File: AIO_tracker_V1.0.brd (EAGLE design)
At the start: 47 x 99.8 mm, 52 parts, among them J1 AVR_SPI_PRG_6PTH, Q1 MOSFET-PCHANNELSMD, U2 USD-SOCKETNEW

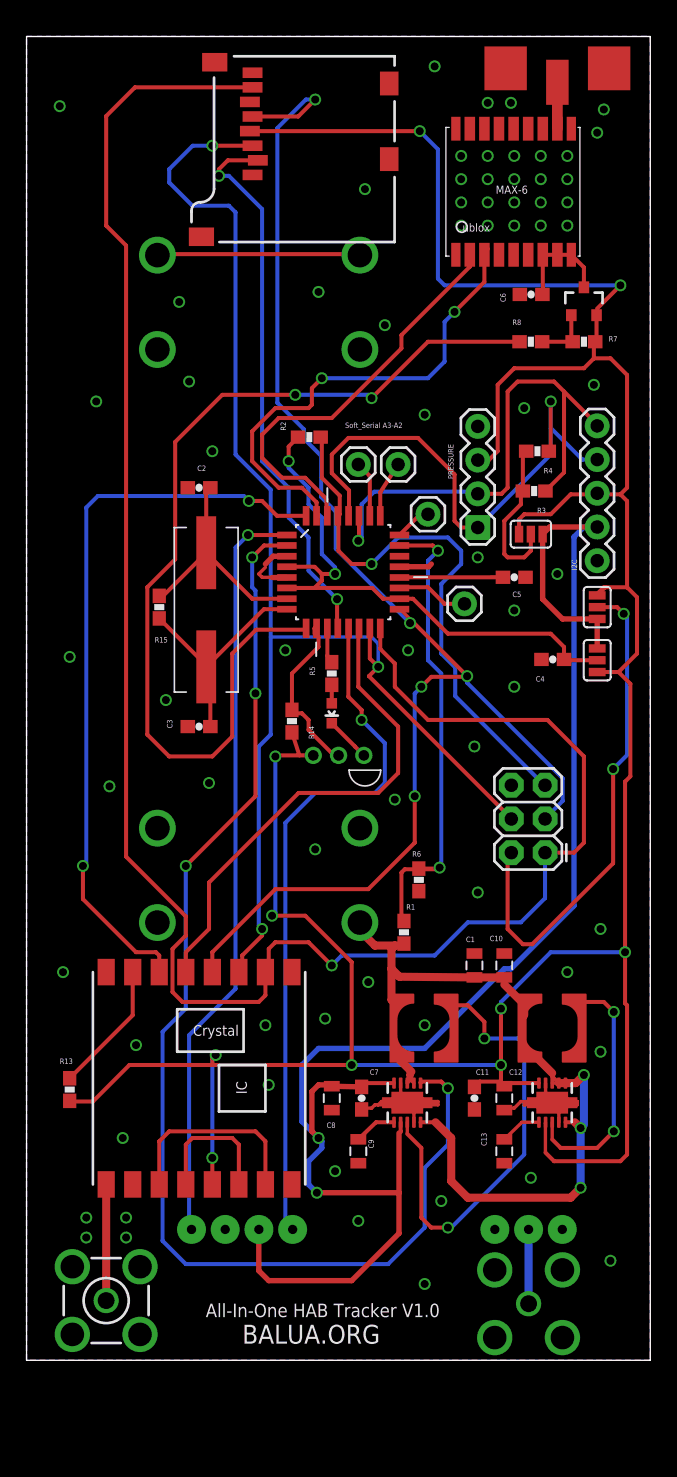
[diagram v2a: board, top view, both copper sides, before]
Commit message: Added extra power pins (5V, 3.3V and GND) and more
Added extra power pins (5V, 3.3V and GND)
Added I2C to Ublox
Placed smd jumpers in both I2C and RX/TX of Ublox for hardware selection
of communication mode.
Added pins for external RX/TX communication with arduino.
PCB layout updated
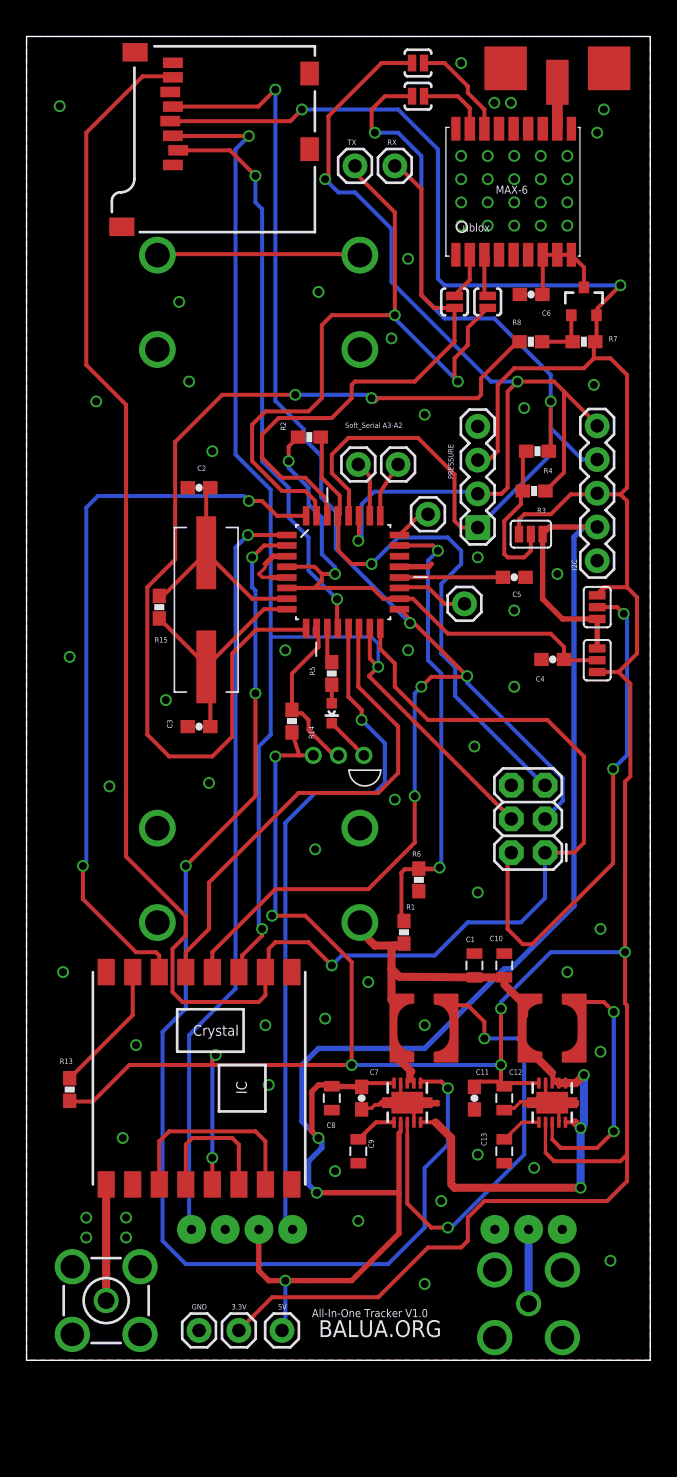
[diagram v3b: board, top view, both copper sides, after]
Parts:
- added 3.3V, 5V, GND, RX, TX: M01PTH, SparkFun-Connectors:1X01
- added SJ1, SJ3, SJ5, SJ6: SOLDERJUMPERNO, SparkFun-Passives:SJ_2S-NO
- moved U2 6.05 mm to (20.7, 80.3)
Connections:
- net D3 renamed SD_CS
- net D4 renamed TEMP
- new net N$11: SJ5.1, U$1.3_RXD1
- new net N$12: SJ6.1, U$1.2_TXD1
- new net N$15: SJ1.2, U$1.16_SDA2
- new net N$16: SJ3.2, U$1.17_SCL2
- net 3.3V: now also 3.3V.1
- net 5V: now also 5V.1
- net GND: now also GND.1
- net SCL: now also SJ3.1
- net SDA: now also SJ1.1
- net UBLOX_RXD: now also SJ5.2, TX.1; no longer U$1.3_RXD1
- net UBLOX_TXD: now also RX.1, SJ6.2; no longer U$1.2_TXD1
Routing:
- net 3.3V: track 250.9 -> 294.9 mm
- net SDA: track 40.5 -> 76.5 mm, vias 1 -> 3
- net SCL: track 43.6 -> 77.9 mm, vias 1 -> 2
- net UBLOX_RXD: track 36.7 -> 53.5 mm
- net UBLOX_TXD: track 31.6 -> 43.4 mm
- net N$15: track 0.00 -> 8.01 mm
- net N$16: track 0.00 -> 5.37 mm
- net MISO: track 150.2 -> 146.0 mm
- net N$11: track 0.00 -> 3.86 mm
- net 5V: track 123.3 -> 127.1 mm, vias 2 -> 3
- net N$12: track 0.00 -> 3.79 mm
- net SCK: track 108.0 -> 110.2 mm
- net MOSI: track 103.1 -> 101.1 mm
- net SD_CS: track 42.0 -> 43.3 mm
- net GPSEN: track 72.5 -> 73.5 mm
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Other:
- board text added: "All-In-One Tracker V1.0"
- board text removed: "All-In-One HAB Tracker V1.0"

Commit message: Updated library and erros
- Ava library updated
- SDN pin of the RFM22b connected to A6 instead of always HIGH
- Updated Sarantel Antenna Footprint
- A7 to external pin
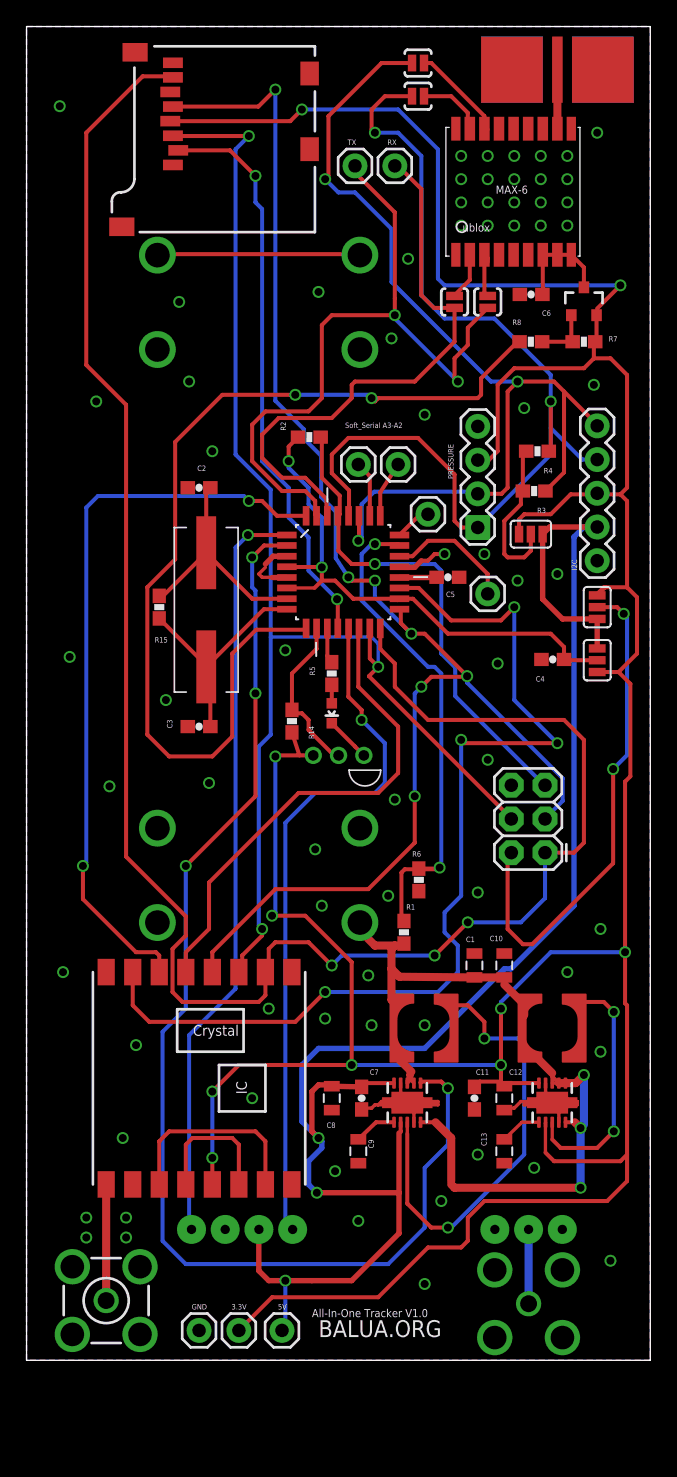
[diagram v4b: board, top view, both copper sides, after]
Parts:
- removed R13: 4.7k, SparkFun-Passives:0603-RES
- C2, C3: value 0.1uF -> 22pF
- R15: value 100k -> 1M
- U$2: value SARANTEL-SL1250 -> JDGA-REMQV-ANTENNA; device Ava:SARANTEL-SL1250 -> Ava:JDGA-RIGID_COMBO_PAD
- moved C5 5.00 mm to (30.8, 40.2)
- moved U$2 2.25 mm to (39.0, 78.5)
- moved JP7 1.90 mm to (33.8, 39.0)
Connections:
- removed net N$27: R13.2, U$7.15
- new net A7: JP7.1, U1.22
- net 3.3V: no longer R13.1
- net A6: now also U$7.15; no longer JP7.1
- net GND: now also U$2.P$2, U$2.P$4, U$2.P$5; no longer U$2.P$1
- net N$3: now also U$2.P$1; no longer U$2.P$2
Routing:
- net A6: track 5.44 -> 76.5 mm, vias 0 -> 4
- net 3.3V: track 294.9 -> 280.1 mm
- net N$27: track 9.97 -> 0.00 mm
- net A7: track 0.00 -> 9.67 mm
- net N$4: track 8.70 -> 2.80 mm
- net RESET: track 41.8 -> 37.1 mm
- net N$8: track 46.8 -> 42.7 mm
- net SCK: track 110.2 -> 112.4 mm, vias 5 -> 7
- net VBATTADC: track 36.4 -> 38.2 mm
- net GND: track 38.0 -> 39.4 mm, vias 72 -> 71
- net N$3: track 3.50 -> 4.45 mm
- net MISO: track 146.0 -> 146.7 mm, vias 1 -> 3
- net N$15: track 8.01 -> 7.43 mm
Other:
- board size 47 x 99.8 mm -> 47 x 100.5 mm

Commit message: Added NTX2 Support option
Added NTX2 Support option and finished routing
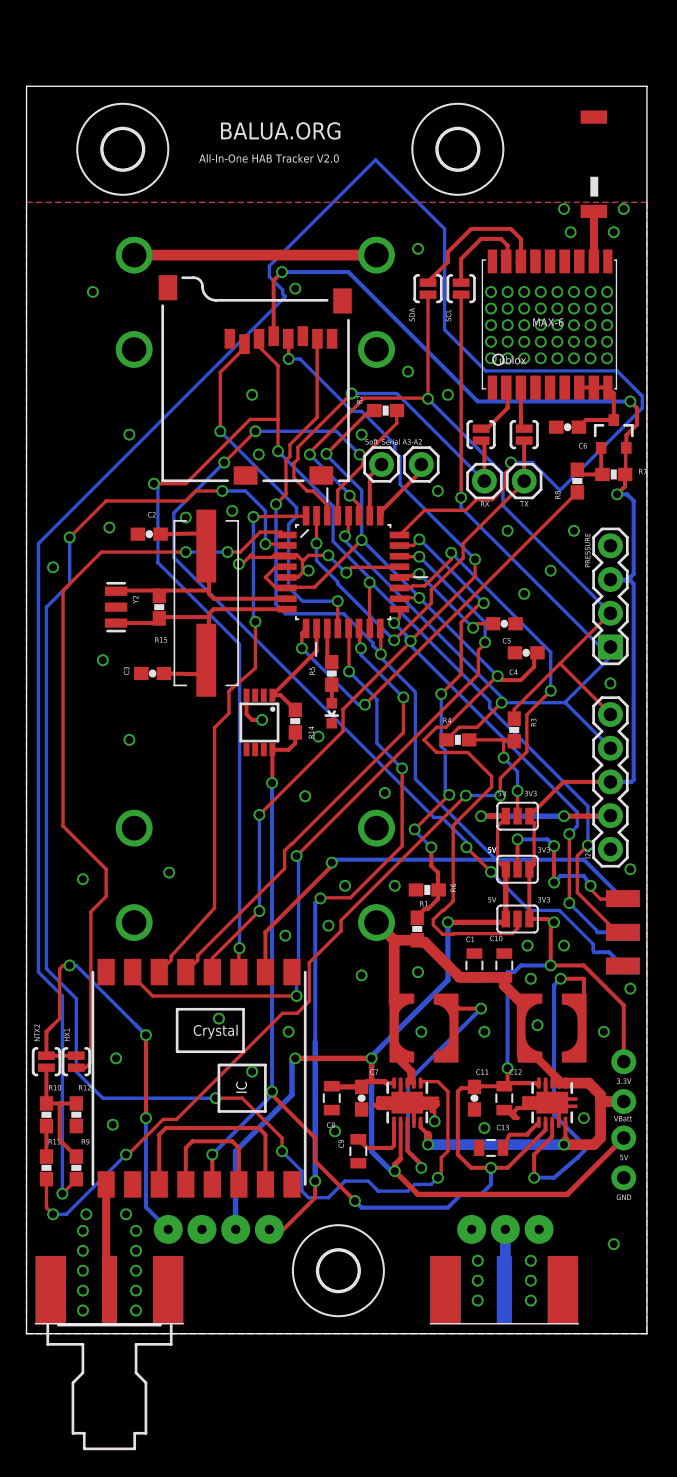
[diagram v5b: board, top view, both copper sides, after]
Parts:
- removed JP4, JP7: M01PTH, SparkFun-Connectors:1X01
- added R10, R11, R12, R9: 10k, SparkFun-Passives:0603-RES
- added SJ2, SJ4: SOLDERJUMPERNO, SparkFun-Passives:SJ_2S-NO
- added U$10, U$11: (no value), holes:3,0
- added VBATT: M01SMDNS, SparkFun-Connectors:1X01NS
- added X1: SMA-142-0701-881/886, con-coax:J502-ND-142-0701-881/886
- added Y2: 16MHz, SparkFun-FreqCtrl:RESONATOR-SMD
- 3.3V, 5V, GND: value M01PTH -> M01SMDNS; device SparkFun-Connectors:1X01 -> SparkFun-Connectors:1X01NS
- J1: value AVR_SPI_PRG_6PTH -> EDGE_ICSP; device SparkFun-Connectors:2X3 -> Ava:EDGE_MOUNTED_ICSP
- JP2, JP3: value JUMPER-3SMD -> (none)
- U$2: value JDGA-REMQV-ANTENNA -> JTI_ANTENNA-1575AT43A40; device Ava:JDGA-RIGID_COMBO_PAD -> Ava:JTI_ANTENNA-1575AT43A40
- U$5: value BUS-SMA -> (none); device Ava:BUS-SMA -> holes:3,0
- U$8: value BUS-SMA -> SMA-142-0701-881/886; device Ava:BUS-SMA -> con-coax:J502-ND-142-0701-881/886
- U$9: value DS1820TO92 -> DS1820; device Ava:DS1820 -> Ava:µSOP8
- moved U$5 87.2 mm to (31.5, 72.5), flipped to the top
- moved 3.3V 35.4 mm to (44.0, 3.75)
- moved GND 34.0 mm to (44.0, -5.00)
- moved U2 32.8 mm to (23.3, 47.5), turned to 0 degrees
- moved 5V 29.6 mm to (44.0, -2.00)
- moved TX 27.0 mm to (36.5, 47.5)
- moved RX 24.7 mm to (33.5, 47.5)
- moved R4 22.6 mm to (31.5, 28.0), turned to 0 degrees
- moved I2C 21.8 mm to (43.0, 19.8)
- moved JP3 21.3 mm to (36.0, 22.2), turned to 180 degrees
- moved JP2 20.6 mm to (36.0, 18.2), turned to 180 degrees
- moved JP1 20.4 mm to (36.0, 14.5), turned to 180 degrees
- moved R3 18.1 mm to (35.8, 28.8), turned to 270 degrees
- moved SJ1 17.0 mm to (29.2, 62.0), turned to 90 degrees
- moved SJ3 14.9 mm to (31.8, 62.0), turned to 90 degrees
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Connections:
- removed net A1: JP4.1, U1.24
- removed net A6: U$7.15, U1.19
- new net MARK: R9.2, U1.24
- new net N$17: R10.1, R12.2, R9.1, SJ4.2
- new net N$18: R10.2, R11.1
- new net SPACE: R11.2, U1.19
- new net TXDHX1NX2: SJ2.1, SJ4.1, U$3.TXD
- net 3.3V: now also U$9.8; no longer U$9.VDD
- net A7: now also U$7.15; no longer JP7.1
- net GND: now also R12.1, U$8.G@1, U$8.G@2, U$8.G@3, U$8.G@4, U$9.4, X1.G@1, X1.G@2, X1.G@3, X1.G@4, Y2.2; no longer U$2.P$2, U$2.P$3, U$2.P$4, U$2.P$5, U$5.2, U$5.3, U$5.4, U$5.5, U$8.2, U$8.3, U$8.4, U$8.5, U$9.GND
- net HX1: now also SJ2.2; no longer U$3.TXD
- net N$20: now also Y2.3
- net N$21: now also Y2.1
- net N$3: now also U$2.FEED; no longer U$2.P$1
- net N$5: now also X1.1; no longer U$5.1
- net TEMP: now also U$9.1; no longer U$9.DQ
- net VBATT: now also VBATT.1
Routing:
- net MARK: track 0.00 -> 149.4 mm, vias 0 -> 2
- net SPACE: track 0.00 -> 80.1 mm, vias 0 -> 6
- net 3.3V: track 280.1 -> 203.5 mm, vias 10 -> 11
- net A6: track 76.5 -> 0.00 mm, vias 4 -> 0
- net MISO: track 146.7 -> 85.4 mm
- net A7: track 9.67 -> 56.1 mm, vias 0 -> 4
- net GPSEN: track 73.5 -> 30.8 mm
- net RESET: track 37.1 -> 77.8 mm, vias 1 -> 5
- net N$8: track 42.7 -> 78.5 mm, vias 2 -> 4
- net TXDHX1NX2: track 0.00 -> 33.3 mm, vias 0 -> 3
- net 5V: track 127.1 -> 97.4 mm, vias 3 -> 6
- net N$9: track 38.4 -> 14.4 mm, vias 2 -> 4
- net UBLOX_RXD: track 53.5 -> 30.9 mm
- net SCK: track 112.4 -> 96.2 mm, vias 7 -> 8
- net SD_CS: track 43.3 -> 27.9 mm
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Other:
- board size 47 x 100.5 mm -> 46.8 x 94 mm
- board text added: "3V3"
- board text added: "5V"
- board text added: "All-In-One HAB Tracker V2.0"
- board text added: "HX1"
- board text added: "NTX2"
- board text added: "SCL"
- board text added: "SDA"
- board text added: "VBatt"
- board text removed: "All-In-One Tracker V1.0"

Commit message: corrected a few erros with the NTX2
Added back pads to the HX1 footprint, corrected the voltage divider,
corrected the antenna layout, changed SDN of RFM22b to the A7, corrected
the values in the schematic

Missing:
- Cuttof system
- New pressure sensor
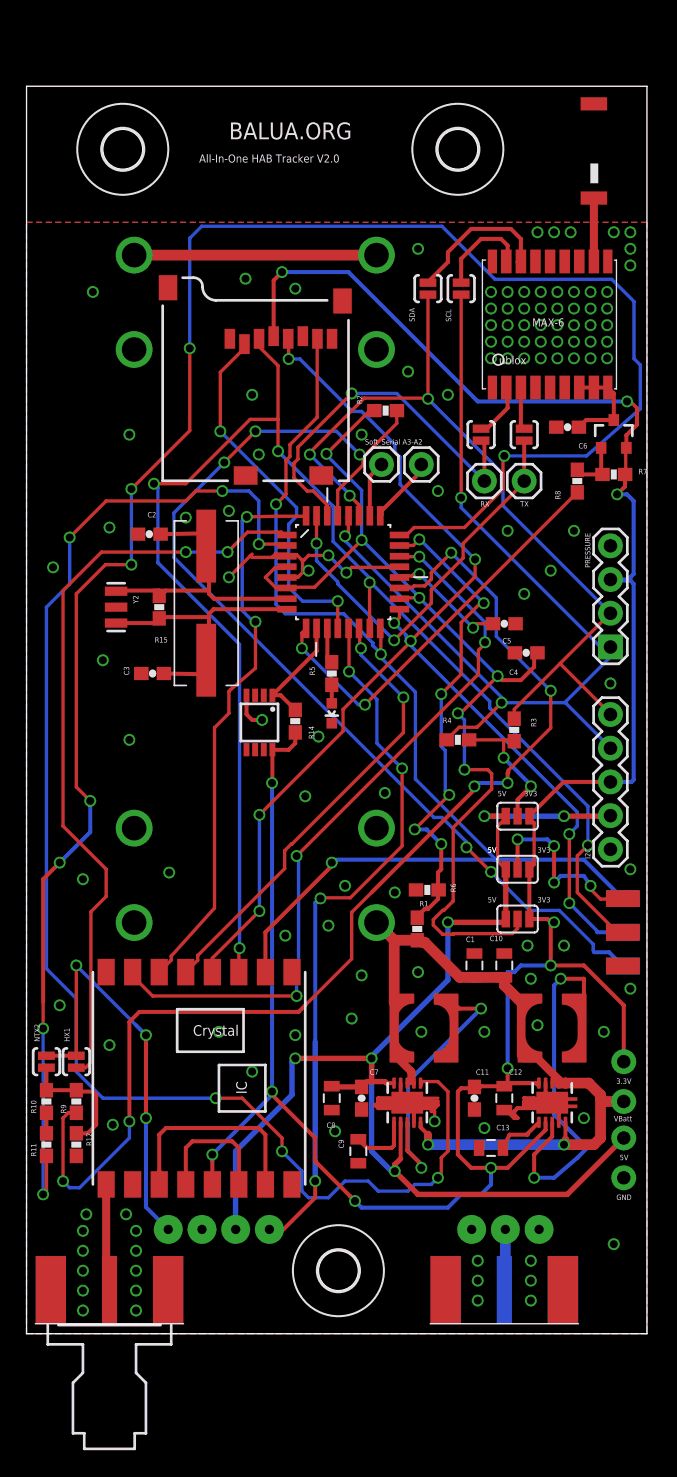
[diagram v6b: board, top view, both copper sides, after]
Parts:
- R10, R9: value 10k -> 22k
- R11: value 10k -> 4.7k
- moved R9 5.00 mm to (2.75, 0.75), turned to 90 degrees
- moved R12 2.25 mm to (2.75, -2.50), turned to 270 degrees
- moved R11 1.75 mm to (0.50, -2.50), turned to 90 degrees
- moved R10 1.00 mm to (0.50, 0.75), turned to 90 degrees
- moved U$2 1.00 mm to (41.8, 72.0)
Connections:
- net GND: now also R12.2; no longer R12.1
- net MARK: now also R11.1; no longer R9.2
- net N$17: now also R10.2, R12.1, R9.2; no longer R10.1, R12.2, R9.1
- net N$18: now also R10.1, R11.2; no longer R10.2, R11.1
- net SPACE: now also R9.1; no longer R11.2
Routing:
- net SPACE: track 80.1 -> 88.1 mm
- net N$8: track 78.5 -> 75.8 mm, vias 4 -> 6
- net N$14: track 9.63 -> 11.9 mm
- net TXDHX1NX2: track 33.3 -> 31.8 mm
- net RFM22_NIRQ: track 41.3 -> 42.7 mm
- net N$18: track 2.80 -> 1.55 mm
- net GND: track 52.5 -> 53.7 mm, vias 118 -> 124
- net N$3: track 3.78 -> 4.78 mm
- net VBATTADC: track 36.6 -> 37.3 mm
- net 5V: track 97.4 -> 96.9 mm
- net MARK: track 149.4 -> 149.8 mm, vias 2 -> 8
